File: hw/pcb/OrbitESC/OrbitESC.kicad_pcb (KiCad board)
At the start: 4 copper layers, 42 x 30 mm, 143 parts, among them J1 USB_C_Receptacle_USB2.0, J11 VDC, J12 GND, J3 TermA, J4 TermB, J5 TermC, J6 CAN1, Q1 MCAC80N10Y, Q2 MCAC80N10Y, Q3 MCAC80N10Y, Q4 MCAC80N10Y, Q5 MCAC80N10Y, Q6 MCAC80N10Y, Q7 2N7002, SW1 Reset, SW2 Boot, U1 TLE9250X, U10 CP2104, U11 STM32L432KBUx, U2 AT25SF081-SSHD-X, U3 24LC128, U4 74HC596, U5 DRV8300DRGER, U6 TSV994, U7 AP62200Z6-7, U8 AP2171W, U9 AP2120

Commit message: Sync PCB updates
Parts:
- removed D3, D4: Blue LED, Diode_SMD:D_0603_1608Metric
- removed D6, D7: Yellow LED, Diode_SMD:D_0603_1608Metric
- removed R17: 39k, Resistor_SMD:R_0402_1005Metric
- removed R20: 1.5k, Resistor_SMD:R_0402_1005Metric
- removed R45: 200, Resistor_SMD:R_0402_1005Metric
- removed R46: 49.9, Resistor_SMD:R_0402_1005Metric
- added C11: 100nF, Capacitor_SMD:C_0402_1005Metric, F.Cu at (153.8, 79.4)
- added C15: 2.2uF, Capacitor_SMD:C_0805_2012Metric, F.Cu at (150.1, 79.9)
- added C30: 1uF, Capacitor_SMD:C_0402_1005Metric, F.Cu at (171.6, 70.3)
- added C31: 100nF, Capacitor_SMD:C_0402_1005Metric, F.Cu at (178.8, 65.8)
- added C32: 100nF, Capacitor_SMD:C_0402_1005Metric, F.Cu at (157.8, 63.8)
- added C33: 2.2uF, Capacitor_SMD:C_0805_2012Metric, F.Cu at (175.1, 76.1)
- added C34: 100nF, Capacitor_SMD:C_0402_1005Metric, F.Cu at (174.3, 78.6)
- added C36: 100nF, Capacitor_SMD:C_0402_1005Metric, F.Cu at (168.5, 78.9)
- added C42: 100nF, Capacitor_SMD:C_0402_1005Metric, F.Cu at (174.5, 68.3)
- added C43: 100nF, Capacitor_SMD:C_0402_1005Metric, F.Cu at (174.5, 70.3)
- added C44: 1uF, Capacitor_SMD:C_0402_1005Metric, F.Cu at (177.4, 68.3)
- added D8: B5819W, Diode_SMD:D_SOD-123, F.Cu at (170.0, 76.3)
- added R30: 10k, Resistor_SMD:R_0402_1005Metric, F.Cu at (178.8, 63.8)
- added R47: 10k, Resistor_SMD:R_0402_1005Metric, F.Cu at (171.6, 68.3)
- added TP1: BL, TestPoint:TestPoint_Pad_D1.0mm, F.Cu at (168.6, 68.8)
- added U12: 74HC595, Package_SO:SOIC-16_3.9x9.9mm_P1.27mm, F.Cu at (152.1, 68.6)
- added U13: TLV9051IDBVR, Package_TO_SOT_SMD:SOT-23-5, F.Cu at (174.8, 65.1)
- added U14: TLV9051IDBVR, Package_TO_SOT_SMD:SOT-23-5, F.Cu at (169.7, 65.1)
- C14: value 2.2uF -> 33nF; footprint Capacitor_SMD:C_0805_2012Metric -> Capacitor_SMD:C_0402_1005Metric
- C16: value 2.2uF -> 100nF; footprint Capacitor_SMD:C_0805_2012Metric -> Capacitor_SMD:C_0402_1005Metric
- C25, C26: value 10uF -> 47uF
- R11: value 39k -> 33
- R16: moved to F.Cu
- R19, R43: value 1.5k -> 10k
- R21, R22: value 10k -> 100k
- R40: value 51k -> 56k
- R5: value 39k -> 2.0k
- R7: value 1.5k -> 470
- R87, R88, R90: value 200 -> 470
- U4: value 74HC596 -> TLV9051IDBVR; footprint Package_SO:TSSOP-16_4.4x5mm_P0.65mm -> Package_TO_SOT_SMD:SOT-23-5
- U6: value TSV994 -> TLV9051IDBVR; footprint Package_SO:TSSOP-14_4.4x5mm_P0.65mm -> Package_TO_SOT_SMD:SOT-23-5
- moved L1 31.1 mm to (192.8, 108.5)
- moved C24 24.6 mm to (185.7, 110.2)
- moved R37 23.8 mm to (188.3, 107.4)
- moved U7 22.0 mm to (184.9, 107.8)
- moved C22 21.9 mm to (187.3, 107.3)
- moved C23 21.2 mm to (187.8, 110.1)
- moved C6 15.7 mm to (181.4, 98.9)
- moved D2 13.8 mm to (185.0, 104.1)
- moved J12 8.04 mm to (175.5, 110.9)
- moved J11 6.62 mm to (168.9, 110.9)
- moved R14 5.84 mm to (173.9, 102.4)
- moved J5 5.66 mm to (175.5, 105.2)
- moved R18 5.62 mm to (161.7, 105.4)
- moved Q5 5.59 mm to (169.2, 104.6)
- moved Q6 5.59 mm to (169.3, 104.6)
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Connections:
- C14 pad 1: Net-(C14-Pad1) -> Net-(U4-Pad2)
- C14 pad 2: GND -> Net-(U4-Pad1)
- C25 pad 1: +5V -> Net-(D8-Pad2)
- C26 pad 1: +5V -> Net-(D8-Pad2)
- L1 pad 2: +5V -> Net-(D8-Pad2)
- R11 pad 1: Net-(Q4-Pad2) -> ISenseVRef
- R11 pad 2: /Outputs and Shunts/B_ISENSE_P -> Net-(U4-Pad1)
- R19 pad 1: +3.3V -> GND
- R19 pad 2: Net-(D6-Pad2) -> LED_nOE
- R27 pad 2: ISenseVRef -> Net-(R27-Pad2)
- R28 pad 1: Net-(C14-Pad1) -> Net-(R27-Pad2)
- R33 pad 2: ISenseVRef -> Net-(R30-Pad1)
- R36 pad 2: ISenseVRef -> Net-(R36-Pad2)
- R40 pad 1: +5V -> Net-(D8-Pad2)
- R5 pad 1: Net-(Q2-Pad2) -> ISenseVRef
- R5 pad 2: /Outputs and Shunts/A_ISENSE_P -> Net-(U4-Pad2)
- R86 pad 1: Net-(D15-Pad2) -> /MCU/Status LEDs/HEARTBEAT
- R86 pad 2: /MCU/Status LEDs/HEARTBEAT -> Net-(D15-Pad2)
- R89 pad 1: Net-(D18-Pad2) -> /MCU/Status LEDs/ARMED
- R89 pad 2: /MCU/Status LEDs/ARMED -> Net-(D18-Pad2)
- U10 pad 13: Net-(D7-Pad1) -> unconnected-(U10-Pad13)
- U10 pad 14: Net-(D6-Pad1) -> unconnected-(U10-Pad14)
- U11 pad 12: unconnected-(U11-Pad12) -> SERIAL1_RST
- U11 pad 2: SERIAL1_RST -> LED_nOE
- U11 pad 21: CAN1_TXD -> CAN1_RXD
- U11 pad 22: CAN1_RXD -> CAN1_TXD
- U4 pad 1: /MCU/Status LEDs/ARMED -> Net-(U4-Pad1)
- U4 pad 2: /MCU/Status LEDs/HEARTBEAT -> Net-(U4-Pad2)
- U4 pad 3: /MCU/Status LEDs/STATUS_0 -> Net-(R21-Pad1)
- U4 pad 4: /MCU/Status LEDs/STATUS_1 -> GND
- U4 pad 5: /MCU/Status LEDs/STATUS_2 -> +3.3VADC
- U6 pad 1: /MCU/MOTOR_IA -> /MCU/MOTOR_IC
- U6 pad 2: Net-(R34-Pad2) -> Net-(R25-Pad2)
- U6 pad 3: ISenseVRef -> Net-(R27-Pad2)
- U6 pad 4: +3.3VADC -> GND
- U6 pad 5: ISenseVRef -> +3.3VADC
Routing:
- net NOR_SCK: track 41.4 -> 103.6 mm, vias 2 -> 5
- net NOR_MOSI: track 42.3 -> 0.00 mm, vias 2 -> 0
- net VDC: track 29.4 -> 4.82 mm, vias 1 -> 0
- net Net-(R27-Pad2): track 0.00 -> 21.4 mm
- net LED_nCS: track 19.9 -> 0.00 mm, vias 1 -> 0
- net /Outputs and Shunts/SH_C: track 16.9 -> 0.74 mm, vias 10 -> 9
- net ISenseVRef: track 14.3 -> 0.00 mm
- net /Outputs and Shunts/GDH_C: track 15.2 -> 3.13 mm, vias 2 -> 1
- net Net-(R40-Pad2): track 12.7 -> 0.76 mm
- net Net-(R34-Pad2): track 11.7 -> 0.00 mm, vias 2 -> 0
- net +3.3VADC: track 20.9 -> 32.6 mm, vias 6 -> 8
- net GND: track 91.5 -> 80.1 mm, vias 44 -> 31
- net unconnected-(U10-Pad14): track 0.00 -> 7.87 mm
- net Net-(D6-Pad1): track 7.87 -> 0.00 mm
- net /Outputs and Shunts/C_ISENSE_P: track 10.1 -> 2.50 mm
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- removed copper zone on F.Cu, net Net-(C24-Pad1)
- removed copper zone on F.Cu, net VDC
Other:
- board text added: "ORBIT ESC V2"
- board text removed: "C"
- board text removed: "ORBIT ESC V1"

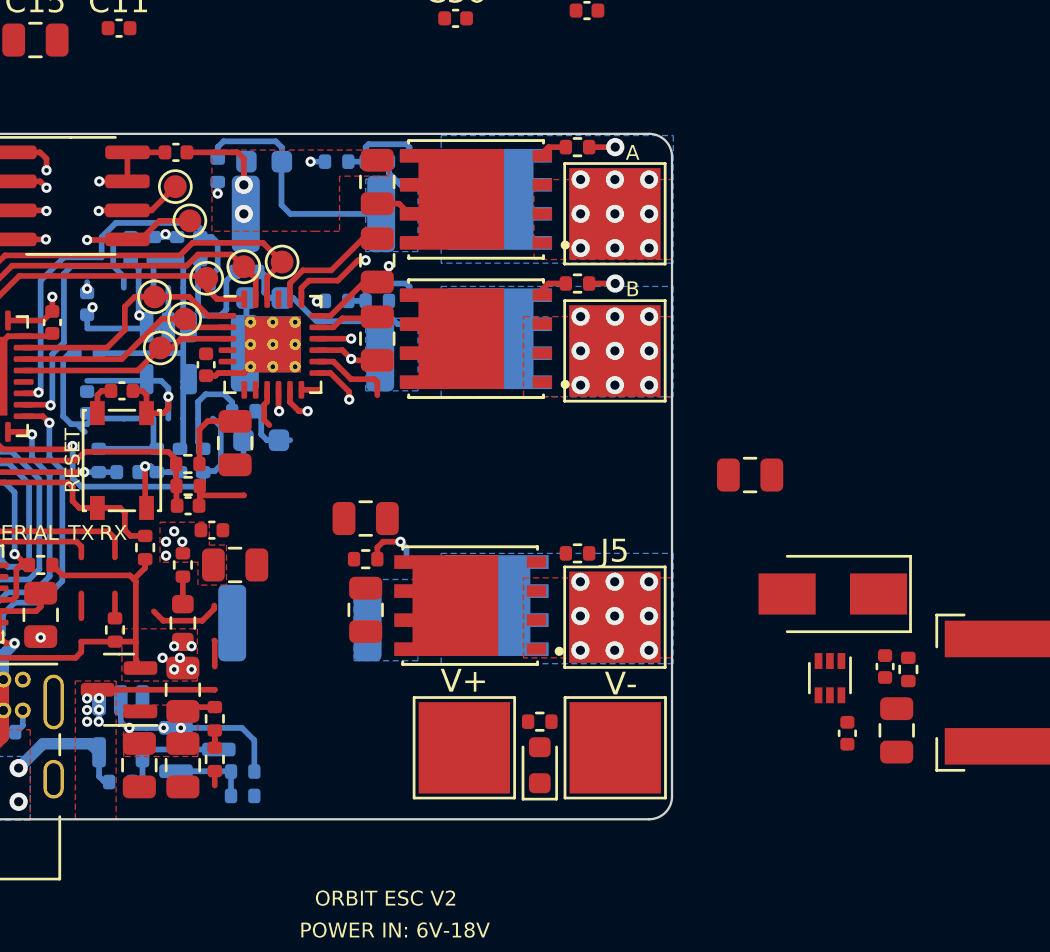
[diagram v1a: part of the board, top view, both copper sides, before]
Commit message: Improve power section layout
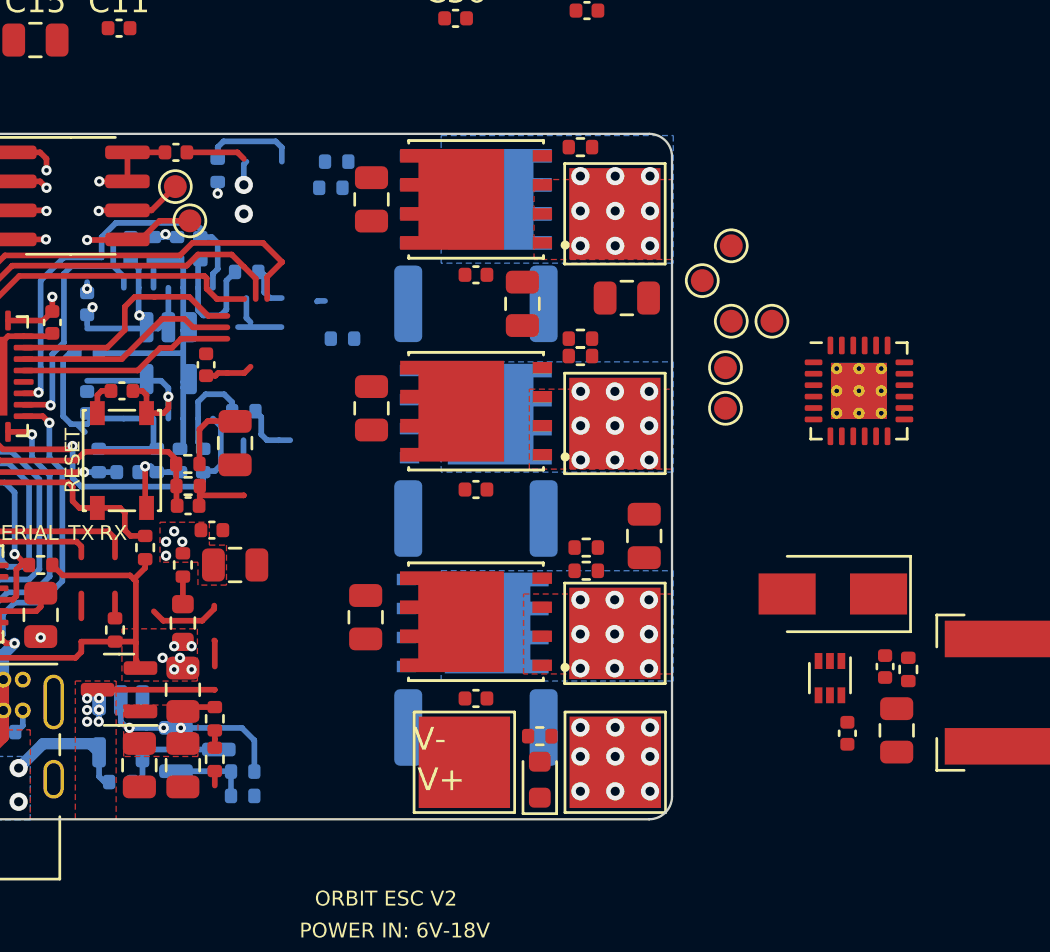
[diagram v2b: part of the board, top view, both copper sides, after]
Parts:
- C2, C5, C8: footprint Capacitor_SMD:C_0603_1608Metric -> Capacitor_SMD:C_0402_1005Metric; moved to F.Cu
- R10: value 10 -> 1; moved to F.Cu
- R14, R16, R2, R4, R8: value 10 -> 1
- moved TP15 27.0 mm to (182.4, 92.2)
- moved U5 25.7 mm to (186.2, 95.2)
- moved TP19 25.4 mm to (180.6, 88.9)
- moved TP17 23.9 mm to (180.6, 92.2)
- moved TP18 23.0 mm to (180.3, 94.2)
- moved TP14 20.4 mm to (180.3, 96.0)
- moved TP16 20.1 mm to (179.3, 90.4)
- moved C6 16.8 mm to (164.8, 96.0), turned to 90 degrees
- moved C8 14.7 mm to (169.4, 108.7), turned to 0 degrees
- moved C5 12.5 mm to (169.4, 99.6), turned to 0 degrees
- moved C21 12.2 mm to (176.8, 101.6), turned to -90 degrees
- moved C19 11.0 mm to (176.0, 91.2), turned to 0 degrees
- moved R10 10.8 mm to (174.0, 93.0), turned to 180 degrees
- moved C2 10.5 mm to (169.4, 90.2), turned to 0 degrees
- moved R12 10.2 mm to (169.4, 100.8), turned to 0 degrees
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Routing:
- net CAN1_TXD: track 30.8 -> 0.00 mm, vias 1 -> 0
- net CAN1_RXD: track 31.8 -> 62.6 mm, vias 1 -> 2
- net /Outputs and Shunts/GDH_A: track 20.1 -> 0.00 mm, vias 2 -> 0
- net Net-(C44-Pad1): track 3.93 -> 20.2 mm, vias 0 -> 1
- net /MCU/Status LEDs/CAN1_ACTV: track 16.3 -> 0.00 mm, vias 1 -> 0
- net /Outputs and Shunts/GDH_B: track 16.0 -> 0.00 mm, vias 2 -> 0
- net /Outputs and Shunts/GDL_A: track 14.1 -> 0.00 mm, vias 2 -> 0
- net /Outputs and Shunts/SH_B: track 13.3 -> 0.00 mm, vias 10 -> 9
- net /Outputs and Shunts/SH_A: track 13.3 -> 0.00 mm, vias 10 -> 9
- net /Outputs and Shunts/A_ISENSE_P: track 12.2 -> 4.15 mm
- net /Outputs and Shunts/B_ISENSE_P: track 9.39 -> 1.95 mm
- net /Outputs and Shunts/GDL_B: track 7.39 -> 0.36 mm, vias 2 -> 0
- net +3.3VADC: track 32.6 -> 27.0 mm, vias 8 -> 7
- net Net-(C19-Pad1): track 5.32 -> 0.00 mm
- net Net-(Q4-Pad2): track 3.79 -> 0.00 mm
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- removed copper zone on B.Cu, net /Outputs and Shunts/A_ISENSE_P
- removed copper zone on B.Cu, net /Outputs and Shunts/B_ISENSE_P
- removed copper zone on B.Cu, net /Outputs and Shunts/C_ISENSE_P
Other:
- board text removed: "A"
- board text removed: "B"

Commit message: Sync work
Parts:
- moved C5 4.83 mm to (174.2, 99.6)
- moved R12 4.66 mm to (174.1, 100.8)
- moved R18 4.66 mm to (174.1, 110.0)
- moved R6 4.66 mm to (174.1, 91.4)
- moved C21 4.07 mm to (180.2, 99.3), turned to 0 degrees
- moved C8 2.29 mm to (171.7, 108.7)
- moved C19 2.05 mm to (174.0, 90.9)
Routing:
- net GND: vias 40 -> 47
- net /Outputs and Shunts/SH_C: vias 9 -> 6
- net /Outputs and Shunts/SH_B: vias 9 -> 6
- net /Outputs and Shunts/SH_A: vias 9 -> 6
- added copper zone on B.Cu, net /Outputs and Shunts/C_ISENSE_P

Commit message: Sync today's work
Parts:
- added C37: 2.2uF, Capacitor_SMD:C_0805_2012Metric, F.Cu at (171.3, 92.1)
- C12, C14, C16, C35, C7, Q7, R11, R13, R21, R22, R25, R26, R27, R28, R29, R31, R32, R33, R34, R35, R36, R38, R39, R4, R44, R5, R62, R9, U4, U6, U8: moved to F.Cu
- U10, U2, U3, U5: moved to B.Cu
- moved U13 59.8 mm to (186.7, 123.7)
- moved U14 59.5 mm to (181.1, 123.4)
- moved C42 59.0 mm to (172.4, 127.3)
- moved C44 59.0 mm to (175.3, 127.3)
- moved C30 59.0 mm to (169.5, 129.2)
- moved C31 59.0 mm to (176.7, 124.8)
- moved C43 59.0 mm to (172.4, 129.2)
- moved R30 59.0 mm to (176.8, 122.8)
- moved R47 59.0 mm to (169.5, 127.3)
- moved TP1 59.0 mm to (166.5, 127.8)
- moved R35 46.9 mm to (179.6, 127.3)
- moved R36 45.3 mm to (199.5, 79.2), turned to 0 degrees
- moved R33 44.7 mm to (199.5, 77.3), turned to 0 degrees
- moved R34 43.9 mm to (196.6, 77.3), turned to 0 degrees
- moved C33 42.6 mm to (152.3, 112.1), turned to -90 degrees
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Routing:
- net NOR_SCK: track 103.6 -> 0.00 mm, vias 5 -> 0
- net GND: track 79.0 -> 8.79 mm, vias 47 -> 23
- net CAN1_RXD: track 62.6 -> 0.00 mm, vias 2 -> 0
- net +3.3V: track 39.3 -> 0.00 mm, vias 16 -> 0
- net +5V: track 30.1 -> 0.00 mm, vias 7 -> 0
- net nRESET: track 28.7 -> 0.00 mm, vias 1 -> 0
- net NOR_nCS: track 27.3 -> 0.00 mm, vias 2 -> 0
- net +3.3VADC: track 27.0 -> 0.00 mm, vias 7 -> 0
- net NOR_MISO: track 24.3 -> 0.00 mm, vias 2 -> 0
- net VBUS: track 21.7 -> 0.00 mm, vias 9 -> 0
- net Net-(R27-Pad2): track 21.4 -> 0.00 mm
- net SERIAL1_IN: track 20.6 -> 0.00 mm, vias 2 -> 0
- net Net-(C44-Pad1): track 20.2 -> 0.00 mm, vias 1 -> 0
- net SERIAL1_OUT: track 19.1 -> 0.00 mm, vias 2 -> 0
- net /MCU/GATE_DRIVE_AH: track 18.0 -> 0.00 mm
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- added copper zone on B.Cu, net /Outputs and Shunts/A_ISENSE_P
- added copper zone on B.Cu, net /Outputs and Shunts/B_ISENSE_P
- added copper zone on F.Cu, net Net-(C24-Pad1)
- added copper zone on F.Cu, net Net-(C25-Pad1)
- added copper zone on F.Cu, net VDC
- removed copper zone on F.Cu, net +3.3V
- removed copper zone on In2.Cu, net +3.3V
- removed copper zone on F.Cu, net +3.3VADC
- removed copper zone on In2.Cu, net +3.3VADC
- removed copper zone on F.Cu, net +5V
- removed copper zone on In2.Cu, net +5V
- removed copper zone on B.Cu, net /Outputs and Shunts/SH_A
- removed copper zone on B.Cu, net /Outputs and Shunts/SH_B
- removed copper zone on B.Cu, net /Outputs and Shunts/SH_C
- removed copper zone on B.Cu, net VBUS
- removed copper zone on F.Cu, net VBUS
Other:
- board text removed: "CAN"
- board text removed: "RX"
- board text removed: "SERIAL"
- board text removed: "SWD"
- board text removed: "TX"

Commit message: Sync lunch work
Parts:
- moved R33 41.4 mm to (163.8, 98.2), turned to 180 degrees
- moved R31 41.2 mm to (160.7, 99.3), turned to -90 degrees
- moved R34 40.2 mm to (160.5, 95.0), turned to -90 degrees
- moved R36 38.7 mm to (163.7, 93.9), turned to 180 degrees
- moved R35 37.8 mm to (161.8, 93.9), turned to 0 degrees
- moved C43 34.0 mm to (165.2, 96.0), turned to -90 degrees
- moved U13 33.2 mm to (163.1, 100.3)
- moved U14 32.9 mm to (162.9, 96.0)
- moved R47 31.5 mm to (160.5, 97.0), turned to -90 degrees
- moved C44 30.9 mm to (155.3, 103.6), turned to -90 degrees
- moved C42 27.8 mm to (165.4, 100.3), turned to -90 degrees
- moved R30 26.8 mm to (160.7, 101.3), turned to 90 degrees
- moved C30 25.8 mm to (159.4, 105.5), turned to -90 degrees
- moved C31 23.1 mm to (165.4, 104.6), turned to -90 degrees
- moved C16 18.1 mm to (155.3, 105.3)
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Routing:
- net VDC: track 18.2 -> 41.0 mm, vias 0 -> 2
- net GND: track 8.79 -> 20.7 mm, vias 23 -> 24
- net VBUS: track 0.00 -> 10.9 mm, vias 0 -> 1
- net +5V: track 0.00 -> 9.39 mm
- net Net-(R40-Pad2): track 0.00 -> 9.15 mm, vias 0 -> 2
- net Net-(Q7-Pad1): track 0.00 -> 5.05 mm
- net +3.3V: track 0.00 -> 4.52 mm
- net Net-(Q7-Pad3): track 0.00 -> 3.68 mm
- net Net-(FB1-Pad2): track 0.00 -> 1.04 mm
- net Net-(C25-Pad1): track 0.00 -> 0.90 mm
- added copper zone on F.Cu, net +5V
